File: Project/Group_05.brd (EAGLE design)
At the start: 80 x 66 mm, 29 parts, among them J1 POWER_JACKPTH_LOCK, U1 +12v, U3 TCA9546A_SMD

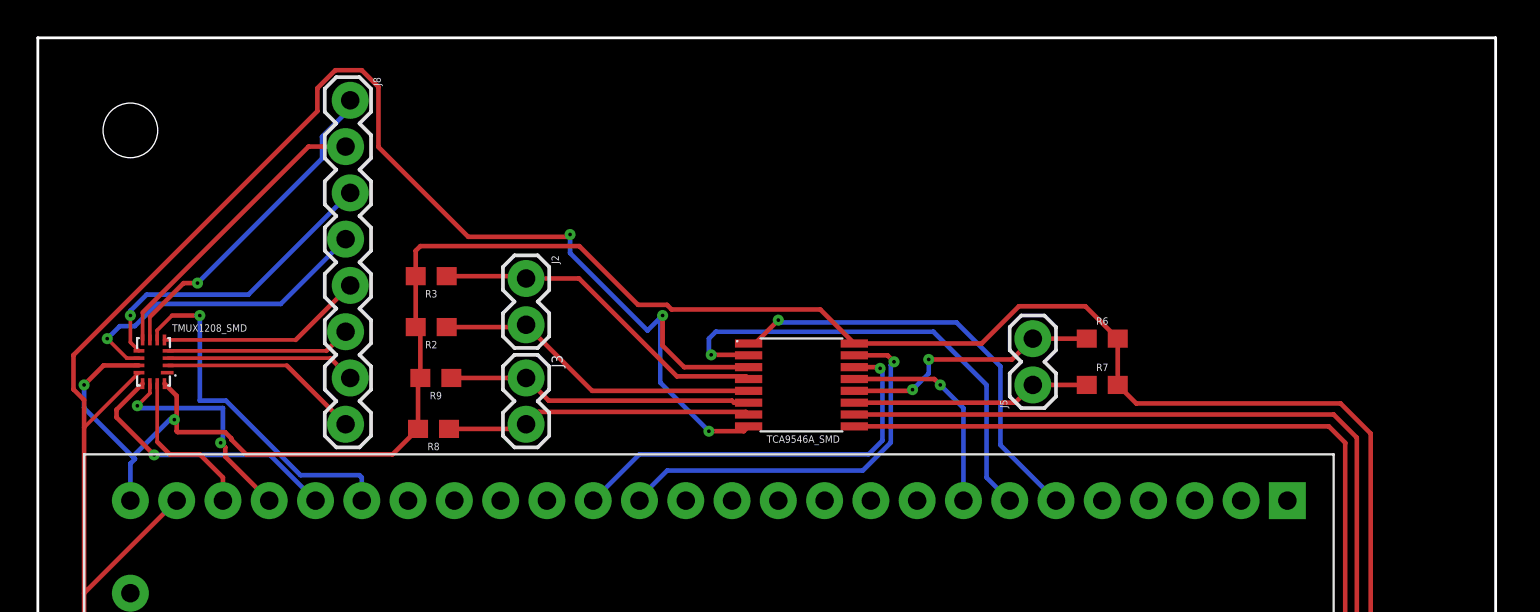
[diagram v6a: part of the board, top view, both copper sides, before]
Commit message: Width 8 mils
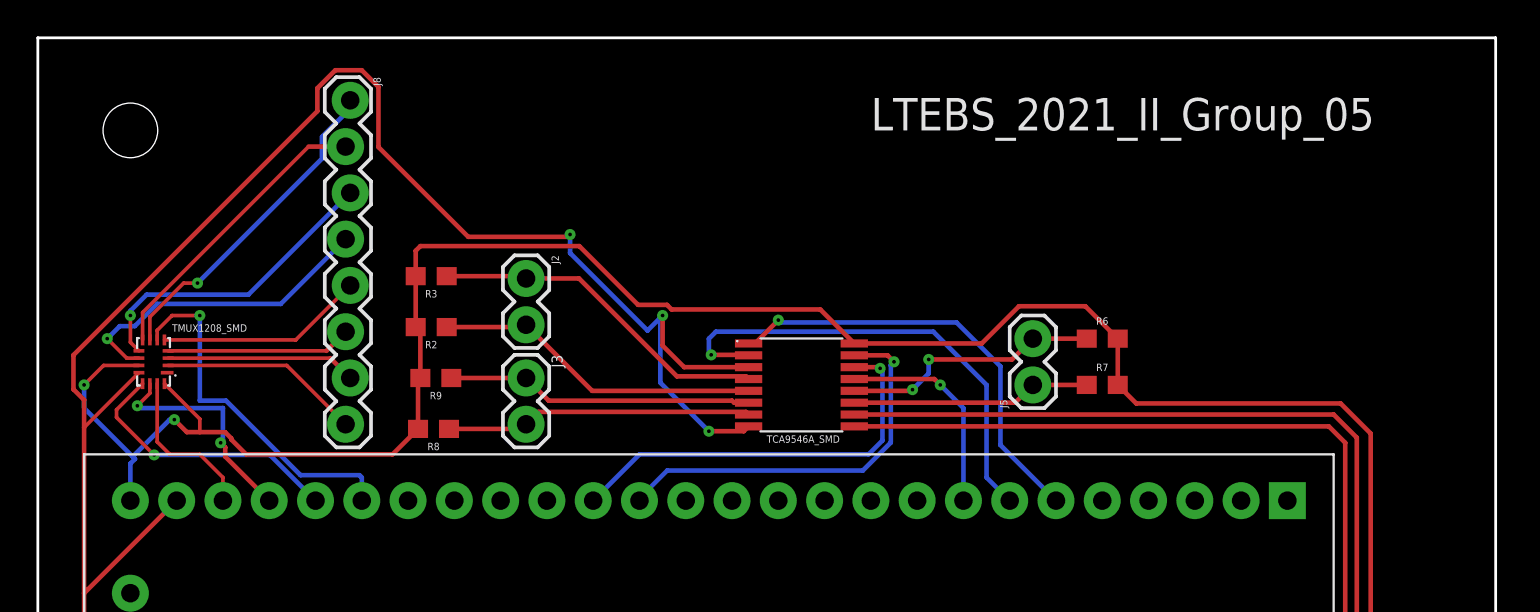
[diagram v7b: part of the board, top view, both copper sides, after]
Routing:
- net 5V: track 202.5 -> 203.3 mm
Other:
- board text added: "LTEBS_2021_II_Group_05"
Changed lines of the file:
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@@
 <text x="6.096" y="51.181" size="0.4064" layer="25" font="vector" ratio="20">TMUX1208_SMD</text>
 <text x="30.48" y="31.75" size="1.778" layer="21" font="vector" ratio="20">CY8CKIT-059</text>
+<text x="44.45" y="62.23" size="1.778" layer="21">LTEBS_2021_II_Group_05</text>
 </plain>
 <attributes>
@@
 <wire x1="19.47" y1="54.229" x2="19.47" y2="55.62513125" width="0.254" layer="1"/>
 <wire x1="19.47" y1="55.62513125" x2="19.72486875" y2="55.88" width="0.254" layer="1"/>
-<wire x1="5.68" y1="48.33" x2="6.35" y2="47.66" width="0.254" layer="1"/>
-<wire x1="6.35" y1="47.66" x2="6.35" y2="46.482" width="0.254" layer="1"/>
-<wire x1="6.35" y1="45.72" x2="6.35" y2="46.482" width="0.254" layer="1"/>
 <via x="6.223" y="46.355" extent="1-16" drill="0.2032"/>
 <wire x1="6.223" y1="46.355" x2="5.969" y2="46.355" width="0.254" layer="16"/>
@@
 <wire x1="1.27" y1="46.99" x2="1.27" y2="48.26" width="0.254" layer="16"/>
 <via x="1.27" y="48.26" extent="1-16" drill="0.2032"/>
-<wire x1="4.28" y1="49.33" x2="2.34" y2="49.33" width="0.254" layer="1"/>
-<wire x1="2.34" y1="49.33" x2="1.27" y2="48.26" width="0.254" layer="1"/>
-<wire x1="6.223" y1="46.355" x2="6.35" y2="46.482" width="0.254" layer="1"/>
+<wire x1="4.28" y1="49.33" x2="2.34" y2="49.33" width="0.2032" layer="1"/>
+<wire x1="2.34" y1="49.33" x2="1.27" y2="48.26" width="0.2032" layer="1"/>
 <wire x1="58" y1="50.8" x2="58" y2="48.3628" width="0.254" layer="1"/>
 <wire x1="58" y1="48.3628" x2="58.0514" y2="48.3114" width="0.254" layer="1"/>
 <wire x1="19.597" y1="45.847" x2="18.2" y2="44.45" width="0.254" layer="1"/>
-<wire x1="18.2" y1="44.45" x2="10.16" y2="44.45" width="0.254" layer="1"/>
-<wire x1="9.3472" y1="45.3269875" x2="9.0049875" y2="45.6692" width="0.254" layer="1"/>
-<wire x1="10.16" y1="44.45" x2="9.3472" y2="45.2628" width="0.254" layer="1"/>
-<wire x1="9.3472" y1="45.2628" x2="9.3472" y2="45.3269875" width="0.254" layer="1"/>
-<wire x1="6.4008" y1="45.6692" x2="6.35" y2="45.72" width="0.254" layer="1"/>
-<wire x1="9.0049875" y1="45.6692" x2="6.4008" y2="45.6692" width="0.254" layer="1"/>
+<wire x1="10.16" y1="44.45" x2="18.2" y2="44.45" width="0.254" layer="1"/>
 <wire x1="33.2619875" y1="52.6542" x2="33.5159875" y2="52.4002" width="0.254" layer="1"/>
 <wire x1="31.6738" y1="52.6542" x2="33.2619875" y2="52.6542" width="0.254" layer="1"/>
@@
 <vertex x="78.74" y="1.27"/>
 </polygon>
+<wire x1="9.0049875" y1="45.6692" x2="9.3472" y2="45.3269875" width="0.254" layer="1"/>
+<wire x1="9.3472" y1="45.3269875" x2="9.3472" y2="45.2628" width="0.254" layer="1"/>
+<wire x1="9.3472" y1="45.2628" x2="10.16" y2="44.45" width="0.254" layer="1"/>
+<wire x1="6.223" y1="46.355" x2="6.9088" y2="45.6692" width="0.254" layer="1"/>
+<wire x1="6.9088" y1="45.6692" x2="7.62" y2="45.6692" width="0.254" layer="1"/>
+<wire x1="7.62" y1="45.6692" x2="9.0049875" y2="45.6692" width="0.254" layer="1"/>
+<wire x1="5.68" y1="48.33" x2="7.62" y2="46.39" width="0.2032" layer="1"/>
+<wire x1="7.62" y1="46.39" x2="7.62" y2="45.6692" width="0.2032" layer="1"/>
 </signal>
 <signal name="PHOTO_OUT">
@@
 <contactref element="U$2" pad="2"/>
 <wire x1="5.88" y1="49.33" x2="12.392" y2="49.33" width="0.2032" layer="1"/>
-<wire x1="12.392" y1="49.33" x2="15.621" y2="46.101" width="0.254" layer="1"/>
+<wire x1="12.392" y1="49.33" x2="15.621" y2="46.101" width="0.2032" layer="1"/>
 </signal>
 <signal name="S2">
@@
 <contactref element="U$2" pad="5"/>
 <wire x1="5.68" y1="50.73" x2="12.884" y2="50.73" width="0.2032" layer="1"/>
-<wire x1="12.884" y1="50.73" x2="15.875" y2="53.721" width="0.254" layer="1"/>
+<wire x1="12.884" y1="50.73" x2="15.875" y2="53.721" width="0.2032" layer="1"/>
 </signal>
 <signal name="S5">
@@
 <wire x1="4.48" y1="50.73" x2="4.48" y2="52.232" width="0.2032" layer="1"/>
 <wire x1="13.589" y1="61.341" x2="15.621" y2="61.341" width="0.254" layer="1"/>
-<wire x1="4.48" y1="52.232" x2="13.589" y2="61.341" width="0.254" layer="1"/>
+<wire x1="4.48" y1="52.232" x2="13.589" y2="61.341" width="0.2032" layer="1"/>
 </signal>
 <signal name="S8">
@@
 <via x="7.493" y="53.848" extent="1-16" drill="0.2032"/>
 <wire x1="4.88" y1="50.73" x2="4.88" y2="51.997" width="0.2032" layer="1"/>
-<wire x1="6.731" y1="53.848" x2="7.493" y2="53.848" width="0.254" layer="1"/>
-<wire x1="4.88" y1="51.997" x2="6.731" y2="53.848" width="0.254" layer="1"/>
+<wire x1="6.731" y1="53.848" x2="7.493" y2="53.848" width="0.2032" layer="1"/>
+<wire x1="4.88" y1="51.997" x2="6.731" y2="53.848" width="0.2032" layer="1"/>
 <wire x1="7.493" y1="53.848" x2="14.3256" y2="60.6806" width="0.254" layer="16"/>
 <wire x1="15.875" y1="63.426975" x2="15.875" y2="63.881" width="0.254" layer="16"/>
@@
 <contactref element="U$1" pad="24"/>
 <wire x1="5.28" y1="48.33" x2="5.28" y2="45.139" width="0.2032" layer="1"/>
-<wire x1="5.969" y1="44.45" x2="7.62" y2="44.45" width="0.254" layer="1"/>
-<wire x1="7.62" y1="44.45" x2="8.89" y2="43.18" width="0.254" layer="1"/>
-<wire x1="8.89" y1="43.18" x2="8.89" y2="41.91" width="0.254" layer="1"/>
-<wire x1="5.28" y1="45.139" x2="5.969" y2="44.45" width="0.254" layer="1"/>
+<wire x1="5.969" y1="44.45" x2="7.62" y2="44.45" width="0.2032" layer="1"/>
+<wire x1="7.62" y1="44.45" x2="8.89" y2="43.18" width="0.2032" layer="1"/>
+<wire x1="8.89" y1="43.18" x2="8.89" y2="41.91" width="0.2032" layer="1"/>
+<wire x1="5.28" y1="45.139" x2="5.969" y2="44.45" width="0.2032" layer="1"/>
 </signal>
 <signal name="MUX_A1/1.4C">
@@
 <contactref element="U$2" pad="13"/>
 <contactref element="U$1" pad="22"/>
-<wire x1="4.48" y1="48.33" x2="3.048" y2="46.898" width="0.254" layer="1"/>
-<wire x1="3.048" y1="46.898" x2="3.048" y2="46.482" width="0.254" layer="1"/>
+<wire x1="4.48" y1="48.33" x2="3.048" y2="46.898" width="0.2032" layer="1"/>
+<wire x1="3.048" y1="46.898" x2="3.048" y2="46.482" width="0.2032" layer="1"/>
 <via x="5.11209375" y="44.41790625" extent="1-16" drill="0.2032"/>
 <wire x1="5.11209375" y1="44.41790625" x2="11.46209375" y2="44.41790625" width="0.254" layer="16"/>
 <wire x1="11.46209375" y1="44.41790625" x2="13.97" y2="41.91" width="0.254" layer="16"/>
-<wire x1="3.048" y1="46.482" x2="5.11209375" y2="44.41790625" width="0.254" layer="1"/>
+<wire x1="3.048" y1="46.482" x2="5.11209375" y2="44.41790625" width="0.2032" layer="1"/>
 </signal>
 <signal name="MUX_OUT/1.4C">
@@
 <wire x1="5.28" y1="50.73" x2="5.28" y2="51.254" width="0.2032" layer="1"/>
 <wire x1="5.28" y1="51.254" x2="6.096" y2="52.07" width="0.2032" layer="1"/>
-<wire x1="6.096" y1="52.07" x2="7.62" y2="52.07" width="0.254" layer="1"/>
+<wire x1="6.096" y1="52.07" x2="7.62" y2="52.07" width="0.2032" layer="1"/>
 <via x="7.62" y="52.07" extent="1-16" drill="0.2032"/>
 <wire x1="16.51" y1="43.18" x2="16.51" y2="41.91" width="0.254" layer="16"/>
